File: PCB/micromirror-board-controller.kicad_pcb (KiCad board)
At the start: 2 copper layers, 74 x 80 mm, 21 parts, among them J1 Barrel_Jack, J2 Conn_01x04_Female, J3 Conn_01x03_Female, J4 Conn_2Rows-51Pins, J5 USB_A, SW1 SW_Push, SW2 SW_Push, U1 Pico, U2 LM1117IMPX-5.0

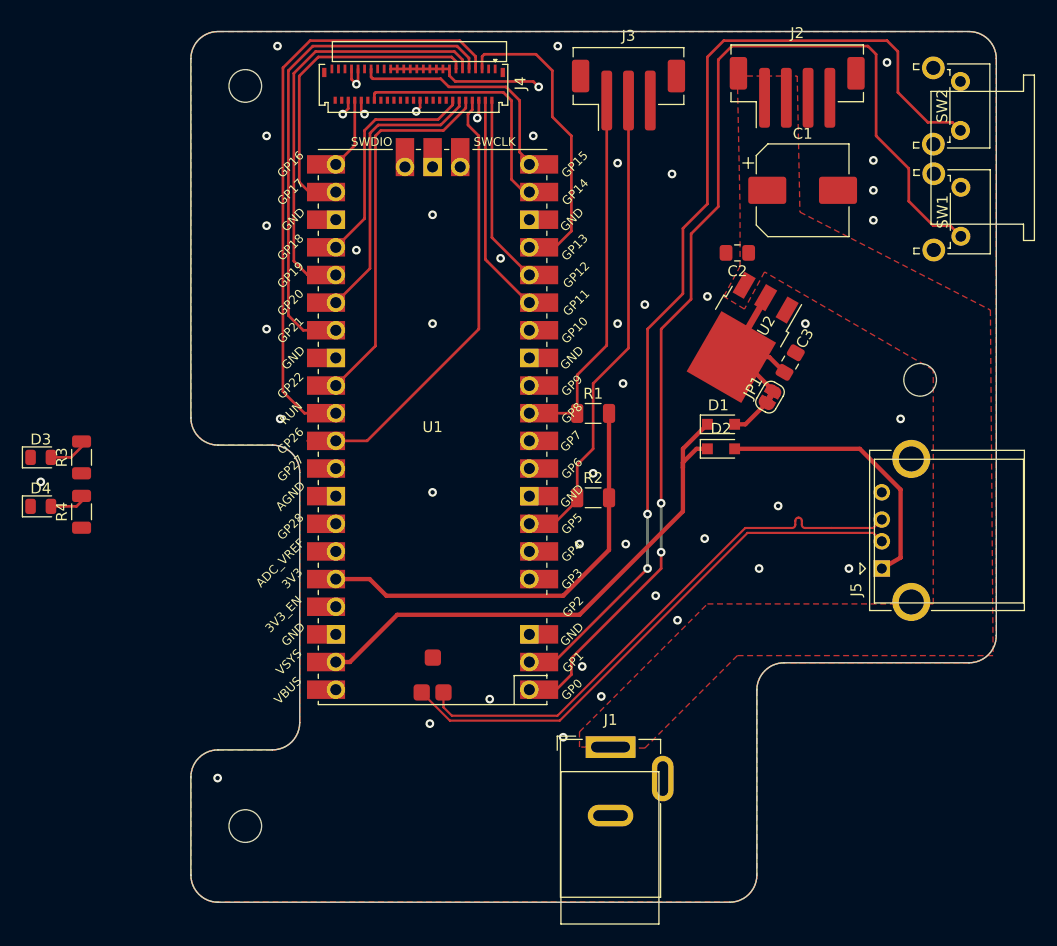
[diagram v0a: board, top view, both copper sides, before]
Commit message: Clean up board silkscreen
Cleaned up silkscreen and added schematic pdf
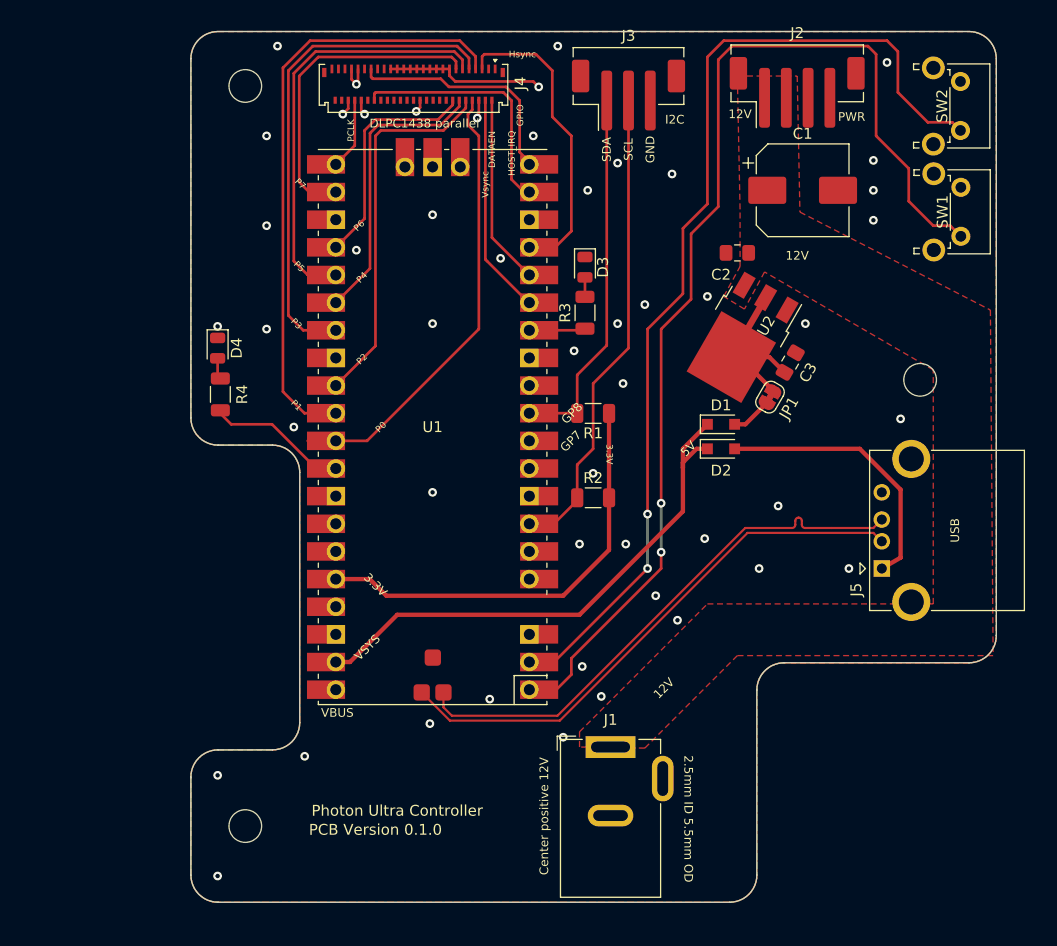
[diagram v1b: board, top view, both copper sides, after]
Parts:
- moved D3 53.0 mm to (151.8, 79.1), turned to -90 degrees
- moved R3 48.1 mm to (151.8, 83.2)
- moved D4 21.8 mm to (118.0, 86.5), turned to -90 degrees
- moved R4 16.7 mm to (118.2, 90.8)
- turned R1 to 180 degrees
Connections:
- R3 pad 1: unconnected-(R3-Pad1) -> Net-(U1-Pad14)
- R4 pad 1: unconnected-(R4-Pad1) -> Net-(U1-Pad32)
- SW1 pad 2: unconnected-(SW1-Pad2) -> Net-(U1-Pad1)
- SW2 pad 2: unconnected-(SW2-Pad2) -> Net-(U1-Pad2)
- U1 pad 1: unconnected-(U1-Pad1) -> Net-(U1-Pad1)
- U1 pad 14: unconnected-(U1-Pad14) -> Net-(U1-Pad14)
- U1 pad 2: unconnected-(U1-Pad2) -> Net-(U1-Pad2)
- U1 pad 32: unconnected-(U1-Pad32) -> Net-(U1-Pad32)
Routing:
- net unconnected-(U1-Pad1): track 102.7 -> 0.00 mm, vias 2 -> 0
- net Net-(U1-Pad1): track 0.00 -> 102.7 mm, vias 0 -> 2
- net unconnected-(U1-Pad2): track 93.2 -> 0.00 mm, vias 2 -> 0
- net Net-(U1-Pad2): track 0.00 -> 93.2 mm, vias 0 -> 2
- net Net-(U1-Pad32): track 0.00 -> 13.0 mm
- net Net-(U1-Pad14): track 0.00 -> 5.17 mm
- net Net-(D3-Pad2): track 3.92 -> 1.79 mm
- net Net-(D4-Pad2): track 3.71 -> 1.95 mm
- net GND: vias 46 -> 50
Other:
- board text added: "12V"
- board text added: "2.5mm ID 5.5mm OD"
- board text added: "3.3V"
- board text added: "5V"
- board text added: "Center positive 12V"
- board text added: "DATAEN"
- board text added: "DLPC1438 parallel"
- board text added: "GND"
- board text added: "GPIO"
- board text added: "HOST_IRQ"
- board text added: "Hsync"
- board text added: "I2C"
- board text added: "P0"
- board text added: "P1"
- board text added: "P2"
- board text added: "P3"
- board text added: "P4"
- board text added: "P5"
- board text added: "P6"
- board text added: "P7"
- board text added: "PCB Version 0.1.0"
- board text added: "PCLK"
- board text added: "PWR"
- board text added: "Photon Ultra Controller"
- board text added: "SCL"
- board text added: "SDA"
- board text added: "USB"
- board text added: "Vsync"

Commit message: Rearrangement of PCB traces and length matching
Needed to rearrange pins. Matched trace lengths; probably overkill.
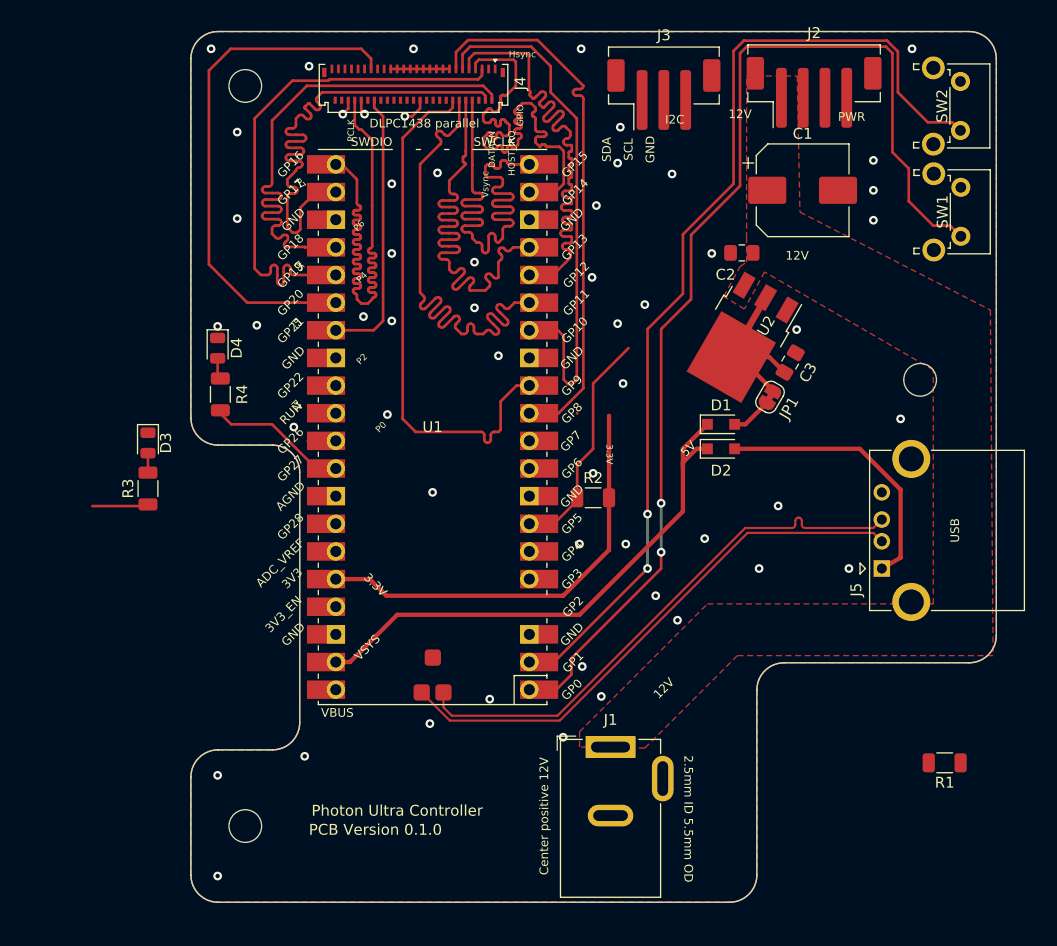
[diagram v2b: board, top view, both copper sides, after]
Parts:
- moved R1 45.5 mm to (184.8, 124.6)
- moved D3 43.3 mm to (111.6, 95.2)
- moved R3 43.3 mm to (111.6, 99.4)
- moved J3 3.25 mm to (159.0, 63.2)
- moved J2 1.55 mm to (172.8, 63.0)
- moved C2 0.41 mm to (166.2, 77.8)
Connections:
- R3 pad 1: Net-(U1-Pad14) -> unconnected-(R3-Pad1)
- U1 pad 11: /SDA -> /P7
- U1 pad 12: unconnected-(U1-Pad12) -> /P6
- U1 pad 14: Net-(U1-Pad14) -> /P5
- U1 pad 15: /Vsync -> /P4
- U1 pad 16: /DATAEN_CMD -> /P3
- U1 pad 17: /Hsync -> /P2
- U1 pad 19: /HOST_IRQ -> /P1
- U1 pad 20: /GPIO 9 -> /P0
- U1 pad 22: /P7 -> /Vsync
- U1 pad 24: /P6 -> /DATAEN_CMD
- U1 pad 25: /P5 -> /Hsync
- U1 pad 26: /P4 -> /GPIO 9
- U1 pad 27: /P3 -> /HOST_IRQ
- U1 pad 29: /P2 -> unconnected-(U1-Pad29)
- U1 pad 30: /P1 -> unconnected-(U1-Pad30)
- U1 pad 31: /P0 -> unconnected-(U1-Pad31)
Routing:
- net /PCLK: track 6.62 -> 48.8 mm
- net /SDA: track 34.5 -> 0.03 mm
- net /DATAEN_CMD: track 17.5 -> 48.9 mm
- net /Vsync: track 20.3 -> 49.1 mm
- net /GPIO 9: track 21.5 -> 48.0 mm
- net /P6: track 23.7 -> 49.1 mm
- net /P4: track 26.7 -> 50.2 mm
- net /SCL: track 44.1 -> 21.3 mm
- net /P7: track 29.5 -> 50.5 mm
- net /Hsync: track 28.3 -> 49.0 mm
- net /P2: track 34.5 -> 49.0 mm
- net GND: track 23.6 -> 10.9 mm, vias 50 -> 54
- net /P5: track 39.1 -> 49.2 mm
- net /P0: track 41.6 -> 51.6 mm
- net /P1: track 55.9 -> 48.8 mm
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
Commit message: Finalised length-matched PCB
Fixed final few remaining traces with the new board layout.
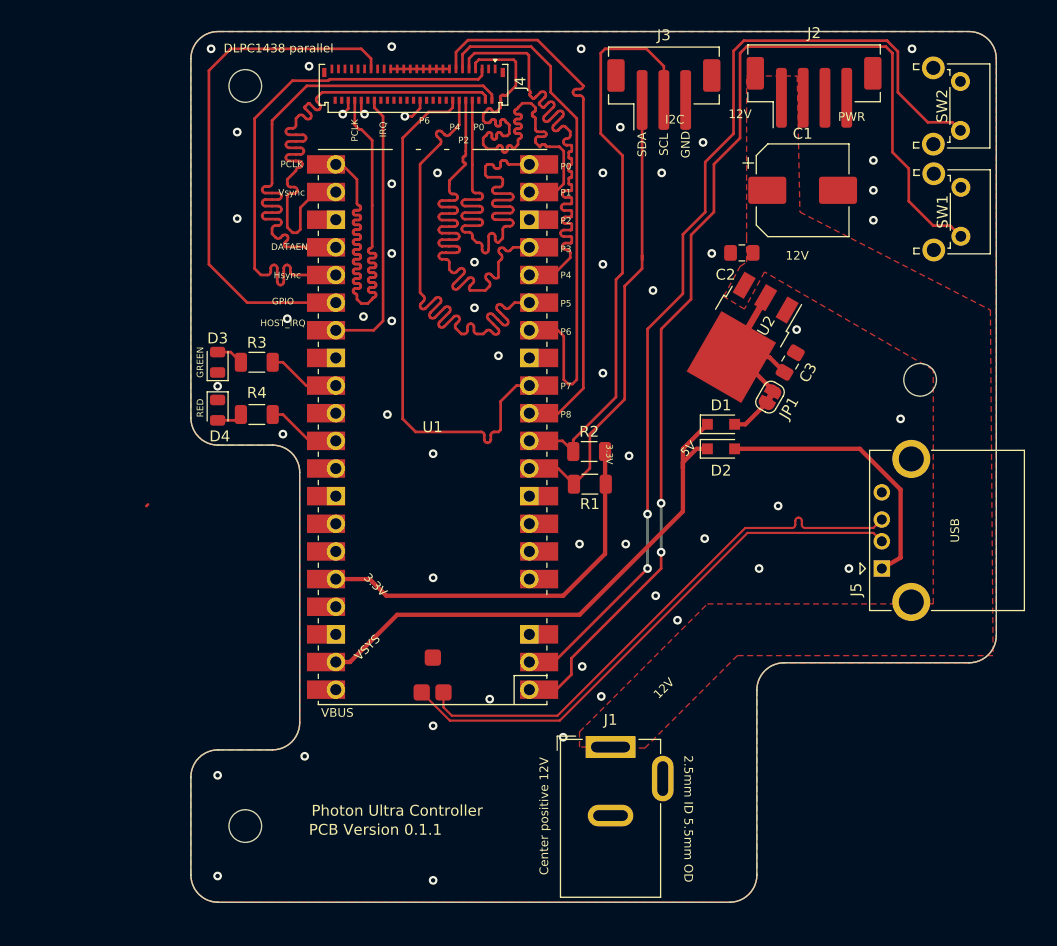
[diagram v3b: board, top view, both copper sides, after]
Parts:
- moved R1 41.5 mm to (152.2, 99.0)
- moved R3 15.3 mm to (121.6, 87.8), turned to 180 degrees
- moved D3 9.79 mm to (118.0, 87.8), turned to 90 degrees
- moved D4 5.70 mm to (118.0, 92.2)
- moved R2 4.27 mm to (152.1, 96.0)
- moved R4 3.83 mm to (121.6, 92.6), turned to 180 degrees
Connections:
- R3 pad 1: unconnected-(R3-Pad1) -> /LED green
- R4 pad 1: Net-(R4-Pad1) -> /LED red
- U1 pad 10: unconnected-(U1-Pad10) -> /SCL
- U1 pad 29: unconnected-(U1-Pad29) -> /LED green
- U1 pad 31: unconnected-(U1-Pad31) -> /LED red
- U1 pad 32: Net-(R4-Pad1) -> unconnected-(U1-Pad32)
- U1 pad 7: /SCL -> unconnected-(U1-Pad7)
- U1 pad 9: unconnected-(U1-Pad9) -> /SDA
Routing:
- net /SDA: track 0.03 -> 43.0 mm
- net /SCL: track 21.3 -> 53.5 mm
- net Net-(R4-Pad1): track 13.0 -> 0.00 mm
- net /LED red: track 0.00 -> 6.80 mm
- net /LED green: track 0.00 -> 6.68 mm
- net unconnected-(R3-Pad1): track 5.17 -> 0.00 mm
- net unconnected-(U1-Pad32): track 0.00 -> 3.50 mm
- net /+3.3V: track 39.8 -> 36.4 mm
- net unconnected-(U1-Pad31): track 2.59 -> 0.00 mm
- net unconnected-(U1-Pad7): track 0.00 -> 2.26 mm
- net Net-(D3-Pad2): track 1.79 -> 2.53 mm
- net GND: vias 54 -> 55
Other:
- board text added: "GREEN"
- board text added: "IRQ"
- board text added: "P8"
- board text added: "PCB Version 0.1.1"
- board text added: "RED"
- board text removed: "PCB Version 0.1.0"

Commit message: Move to USB-C connector
Replacing the original type-A connector now a type-C connector. CC1/2 terminated with 5.1k.
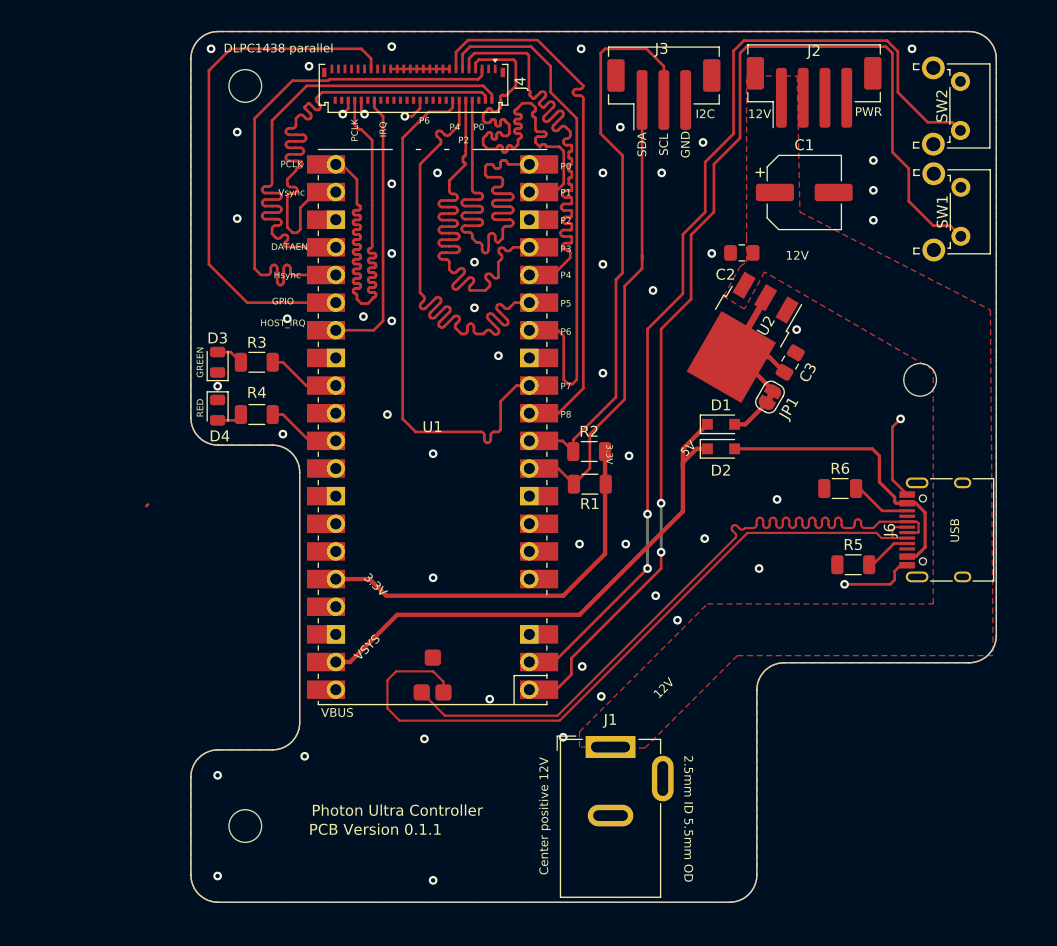
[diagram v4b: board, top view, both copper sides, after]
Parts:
- removed J5: USB_A, Connector_USB:USB_A_CONNFLY_DS1095-WNR0
- added J6: USB_C_Receptacle_USB2.0, Connector_USB:USB_C_Receptacle_HRO_TYPE-C-31-M-12, F.Cu at (185.4, 103.2)
- added R5: 5.1K, Resistor_SMD:R_1206_3216Metric, F.Cu at (176.4, 106.4)
- added R6: 5.1K, Resistor_SMD:R_1206_3216Metric, F.Cu at (175.2, 99.4)
- C1: footprint Capacitor_SMD:CP_Elec_8x10 -> Capacitor_SMD:CP_Elec_6.3x7.7
- moved C1 0.25 mm to (171.9, 72.2)
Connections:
- D2 pad 2: Net-(D2-Pad2) -> /VBUS-C
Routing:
- net /VBUS-C: track 0.00 -> 26.8 mm
- net Net-(D2-Pad2): track 25.0 -> 0.00 mm
- net /D-: track 50.8 -> 67.6 mm
- net /D+: track 50.8 -> 67.3 mm
- net GND: track 10.9 -> 25.6 mm
- net Net-(J6-PadB5): track 0.00 -> 5.54 mm
- net Net-(J6-PadA5): track 0.00 -> 4.30 mm

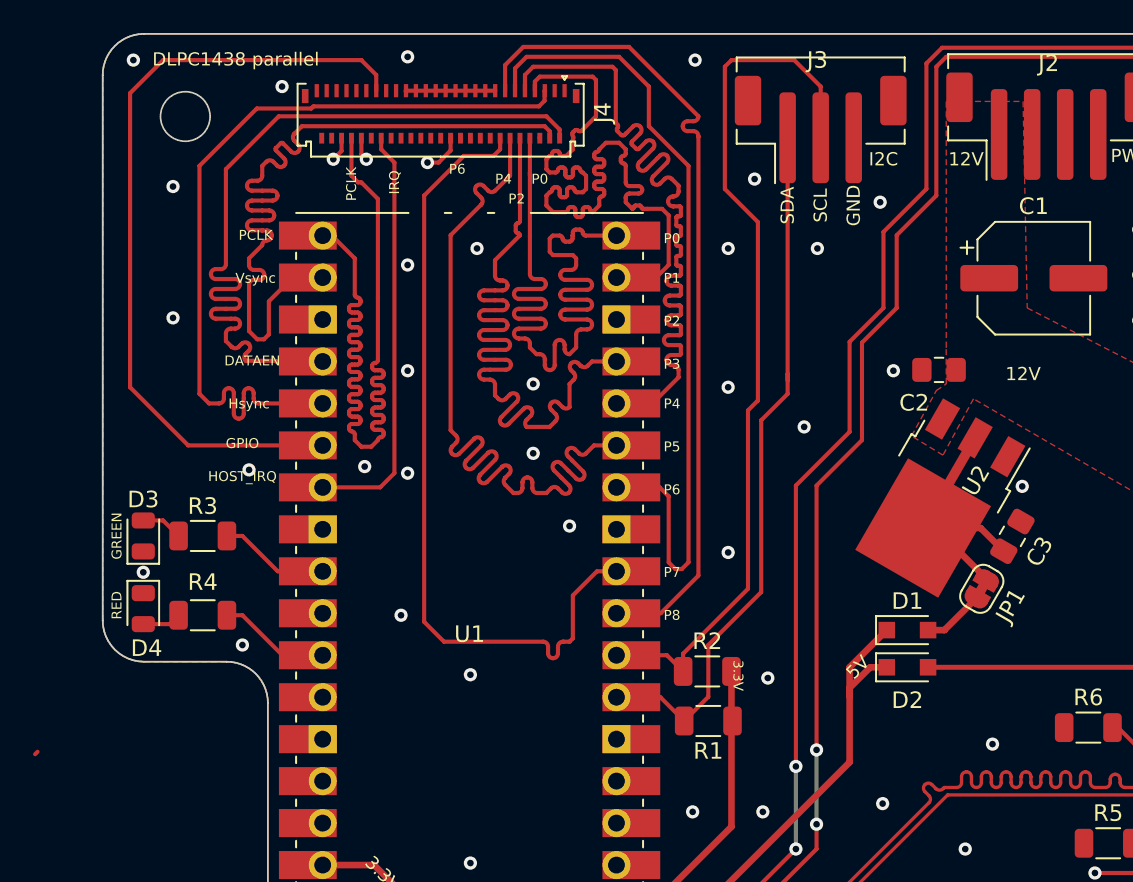
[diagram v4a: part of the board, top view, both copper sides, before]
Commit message: Add openMLA logo
Added logo and fixed missing ground connection on FPC. Did some cleanup with DRC.
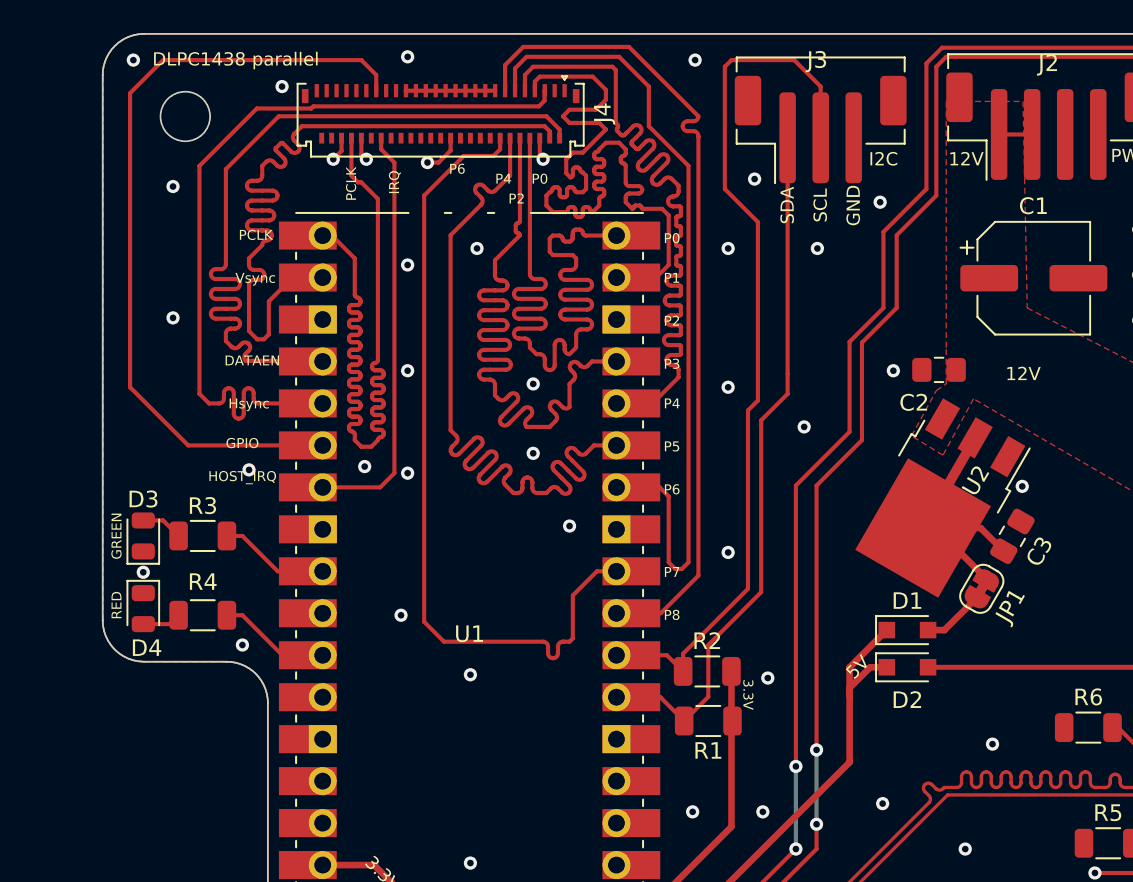
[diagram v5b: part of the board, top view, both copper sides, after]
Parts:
- added G***: LOGO, openMLA-logo, B.Cu at (165.8, 88.2)
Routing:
- net unconnected-(U1-Pad32): track 3.50 -> 0.00 mm
- net unconnected-(U1-Pad7): track 2.26 -> 0.00 mm
- net /+12V: track 0.00 -> 2.00 mm
- net /P1: track 48.8 -> 50.5 mm
- net GND: track 25.6 -> 26.9 mm, vias 55 -> 56
- net /+5V VSYS: track 50.9 -> 49.8 mm
- net /P0: track 51.6 -> 50.8 mm
